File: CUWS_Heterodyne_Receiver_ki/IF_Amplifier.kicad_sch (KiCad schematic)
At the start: 0 parts

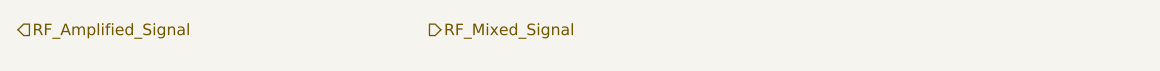
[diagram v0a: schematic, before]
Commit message: Finalised first draft of top hierarchy
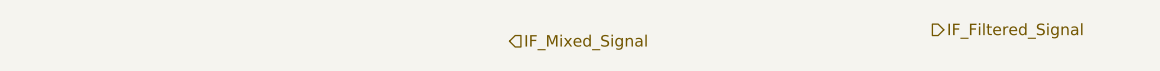
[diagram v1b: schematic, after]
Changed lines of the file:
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@@
 	(generator_version "8.0")
 	(paper "A4")
-	(hierarchical_label "RF_Amplified_Signal"
+	(hierarchical_label "IF_Mixed_Signal"
 		(shape input)
-		(at 50.8 81.28 0)
+		(at 105.41 82.55 0)
 		(fields_autoplaced yes)
 		(effects
@@
 		)
 	)
-	(hierarchical_label "RF_Mixed_Signal"
+	(hierarchical_label "IF_Filtered_Signal"
 		(shape output)
-		(at 96.52 81.28 0)
+		(at 152.4 81.28 0)
 		(fields_autoplaced yes)
 		(effects
